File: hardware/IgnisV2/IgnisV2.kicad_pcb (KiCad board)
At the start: 2 copper layers, 50 x 50 mm, 82 parts, among them J1 COIL_A, J2 COIL_B, J3 530480210, J4 Conn_01x01_Pin, SW1 SW-18030, U1 BQ51013BRHLT, U2 BQ24073RGTR, U3 FP6277XR-G1, U4 74LVC1G17, U5 ATtiny212-SS

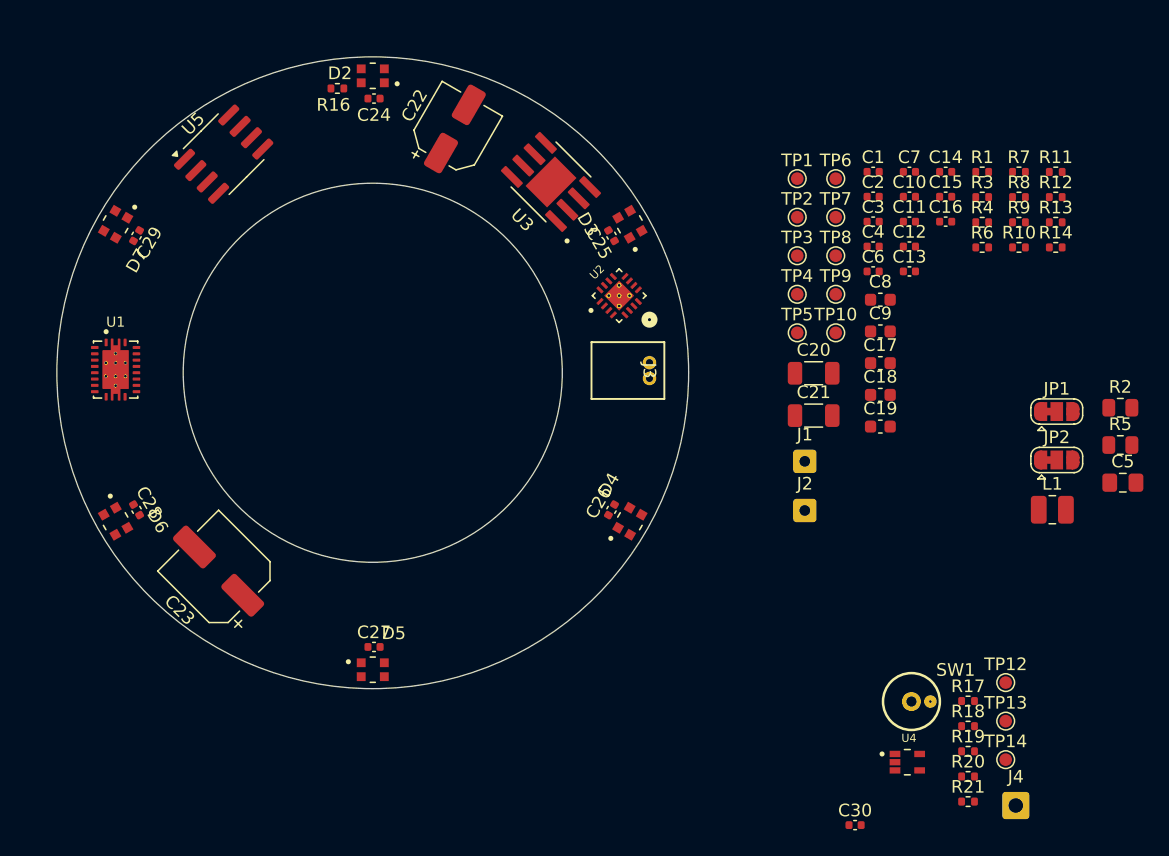
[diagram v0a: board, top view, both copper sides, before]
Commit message: 🏭 Finalize IgnisV2 PCB design and prepare for JLCPCB production
- Polished hierarchical schematics with clean signal routing
- Completed full PCB layout with optimized component placement
- Refined component selection for optimal JLCPCB compatibility
- Generated production files (Gerbers, drill, BOM, pick&place) for fabrication
- Exported 3D model snapshot for documentation and review
- Added 74LVC1G17 datasheet for package selection reference
- Selected TSSOP-5 package over SOT1202 for PCBA compatibility
- Configured for advanced PCBA service due to WS2812B backing requirements
- Updated design rules and gitignore for production workflow
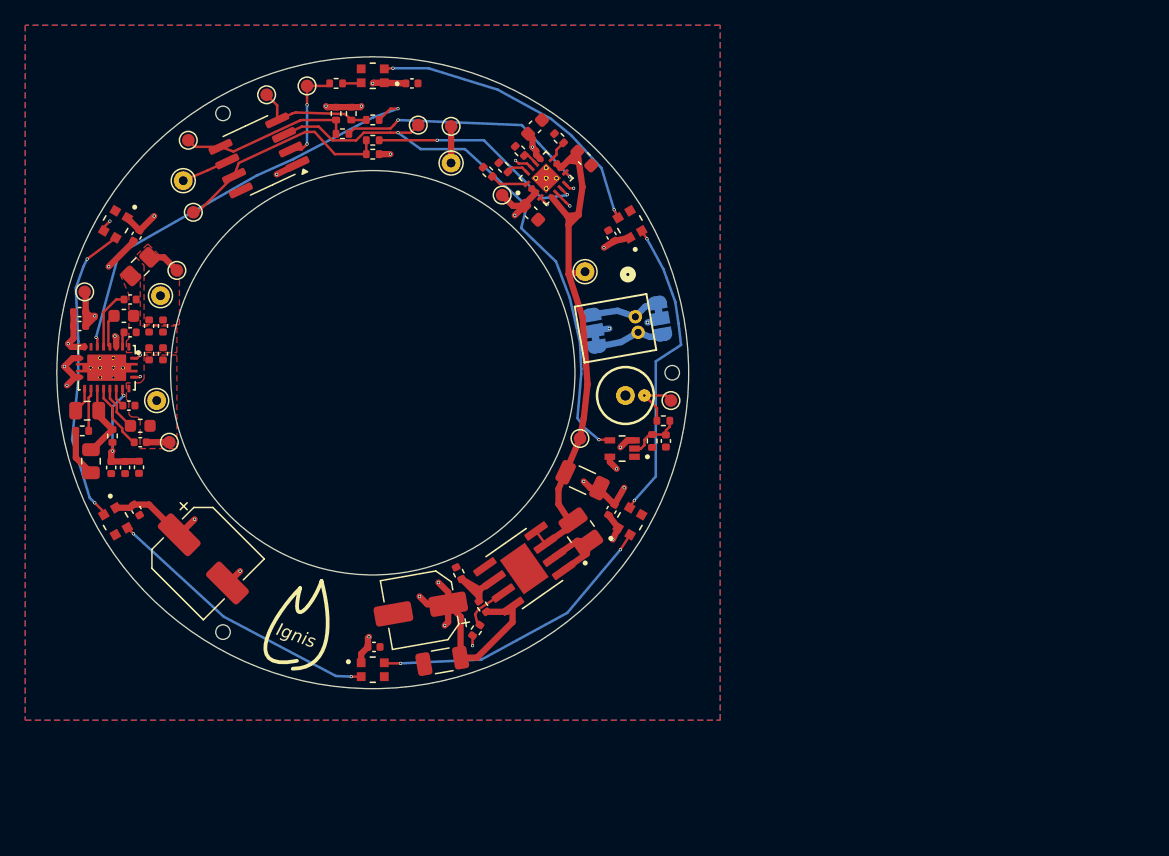
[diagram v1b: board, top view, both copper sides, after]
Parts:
- removed TP10: FB, TestPoint:TestPoint_Pad_D1.0mm
- added H1: ToolingHole, MountingHole:ToolingHole_1.152mm, F.Cu at (73.7, 50.0)
- added H2: ToolingHole, MountingHole:ToolingHole_1.152mm, F.Cu at (38.1, 70.5)
- added H3: ToolingHole, MountingHole:ToolingHole_1.152mm, F.Cu at (38.1, 29.5)
- added J5: VSYS, TestPoint:TestPoint_THTPad_D1.5mm_Drill0.7mm, F.Cu at (66.8, 42.0)
- added J6: GND, TestPoint:TestPoint_THTPad_D1.5mm_Drill0.7mm, F.Cu at (56.2, 33.4)
- J1, J2: footprint Connector_Wire:SolderWire-0.25sqmm_1x01_D0.65mm_OD1.7mm -> TestPoint:TestPoint_THTPad_D1.5mm_Drill0.7mm
- J4: value Conn_01x01_Pin -> UPDI; footprint Connector_Wire:SolderWire-0.5sqmm_1x01_D0.9mm_OD2.1mm -> TestPoint:TestPoint_THTPad_D1.5mm_Drill0.7mm
- JP1: value VGNDC -> VBATS; moved to B.Cu
- JP2: value VBATC -> VGNDS; moved to B.Cu
- moved J4 82.4 mm to (35.0, 34.8)
- moved R2 81.8 mm to (27.4, 53.0)
- moved R5 81.5 mm to (27.7, 57.0), turned to -90 degrees
- moved C5 79.6 mm to (31.6, 41.6), turned to -135 degrees
- moved R3 73.6 mm to (27.0, 54.6), turned to 180 degrees
- moved TP12 72.7 mm to (44.8, 27.3)
- moved R20 72.5 mm to (47.1, 29.5), turned to -90 degrees
- moved R4 70.9 mm to (29.4, 55.0), turned to 90 degrees
- moved R19 70.2 mm to (48.3, 29.5), turned to -90 degrees
- moved R21 69.6 mm to (50.0, 32.7), turned to 180 degrees
- moved C15 69.3 mm to (26.8, 46.3), turned to 180 degrees
- moved C16 68.9 mm to (26.8, 45.2), turned to 180 degrees
- moved TP14 68.4 mm to (53.6, 30.4)
- moved C14 68.0 mm to (31.5, 57.5), turned to -90 degrees
- moved C13 65.1 mm to (29.3, 57.5), turned to -90 degrees
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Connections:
- net Net-(J1-Pin_1) renamed /Power Stage/COILA
- net Net-(J2-Pin_1) renamed /Power Stage/AC2
- net Net-(JP1-C) renamed VBAT
- net Net-(U1-AC1) renamed /Power Stage/AC1
- J3 pad 1: Net-(JP1-A) -> Net-(J3-GND)
- J3 pad 2: Net-(JP1-B) -> Net-(J3-VBAT)
- JP1 pad 1: Net-(JP1-A) -> Net-(J3-VBAT)
- JP1 pad 3: Net-(JP1-B) -> Net-(J3-GND)
- JP2 pad 1: Net-(JP1-B) -> Net-(J3-GND)
- JP2 pad 3: Net-(JP1-A) -> Net-(J3-VBAT)
- R21 pad 2: ~{STBY} -> ~{PGOOD}
- R9 pad 2: ~{STBY} -> ~{PGOOD}
- TP12 pad 1: Net-(D2-DIN) -> LED_DIN
- U2 pad 18: (no net) -> GND
- U2 pad 19: (no net) -> GND
- U2 pad 20: (no net) -> GND
- U2 pad 21: (no net) -> GND
- U2 pad 22: (no net) -> GND
- U5 pad 7: ~{STBY} -> ~{PGOOD}
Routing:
- net VBUS: track 0.00 -> 55.9 mm, vias 0 -> 3
- net VCC: track 0.00 -> 46.8 mm, vias 0 -> 14
- net SSW: track 0.00 -> 45.7 mm, vias 0 -> 2
- net VSYS: track 0.00 -> 42.7 mm
- net Net-(U1-~{CHG}): track 0.00 -> 34.4 mm, vias 0 -> 2
- net GND: track 0.00 -> 33.6 mm, vias 0 -> 17
- net Net-(D3-DOUT): track 0.00 -> 24.4 mm, vias 0 -> 2
- net Net-(D6-DOUT): track 0.00 -> 24.0 mm, vias 0 -> 2
- net Net-(D2-DOUT): track 0.00 -> 23.8 mm, vias 0 -> 2
- net Net-(D4-DOUT): track 0.00 -> 23.4 mm, vias 0 -> 2
- net Net-(D5-DOUT): track 0.00 -> 22.4 mm, vias 0 -> 2
- net Net-(U2-~{CHG}): track 0.00 -> 20.3 mm, vias 0 -> 2
- net VBAT: track 0.00 -> 18.2 mm, vias 0 -> 2
- net ~{PGOOD}: track 0.00 -> 18.0 mm
- net Net-(U2-~{PGOOD}): track 0.00 -> 17.5 mm, vias 0 -> 2
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- added copper zone on F.Cu, net /Power Stage/AC1
- added copper zone on F.Cu, net /Power Stage/AC2
- added copper zone on F.Cu, net /Power Stage/COILA
- added copper zone on B.Cu, net GND
- added copper zone on F.Cu, net GND
- added copper zone on In1.Cu, net GND
- added copper zone on In2.Cu, net VBUS
- added copper zone on In2.Cu, net VCC
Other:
- outline, holes or cut-outs redrawn
- copper layers 2 -> 4
- board text added: "Ignis"
- board text added: "Ignis - V2.0 Théo - 2025-08-25"

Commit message: 🚨 Fix critical PCB issues caught during JLCPCB review
- Fixed undersized vias (<0.3mm) in component footprints to avoid extra costs
- Corrected WS2812B symbol pinout mismatch between standard and 2020 package
- Updated WS2812B-2020 wiring to match proper pin assignments
- Regenerated production files with corrected drill sizes and routing

**Critical catch: WS2812B standard vs 2020 package have different pinouts!**

Production halted and corrected before fabrication.
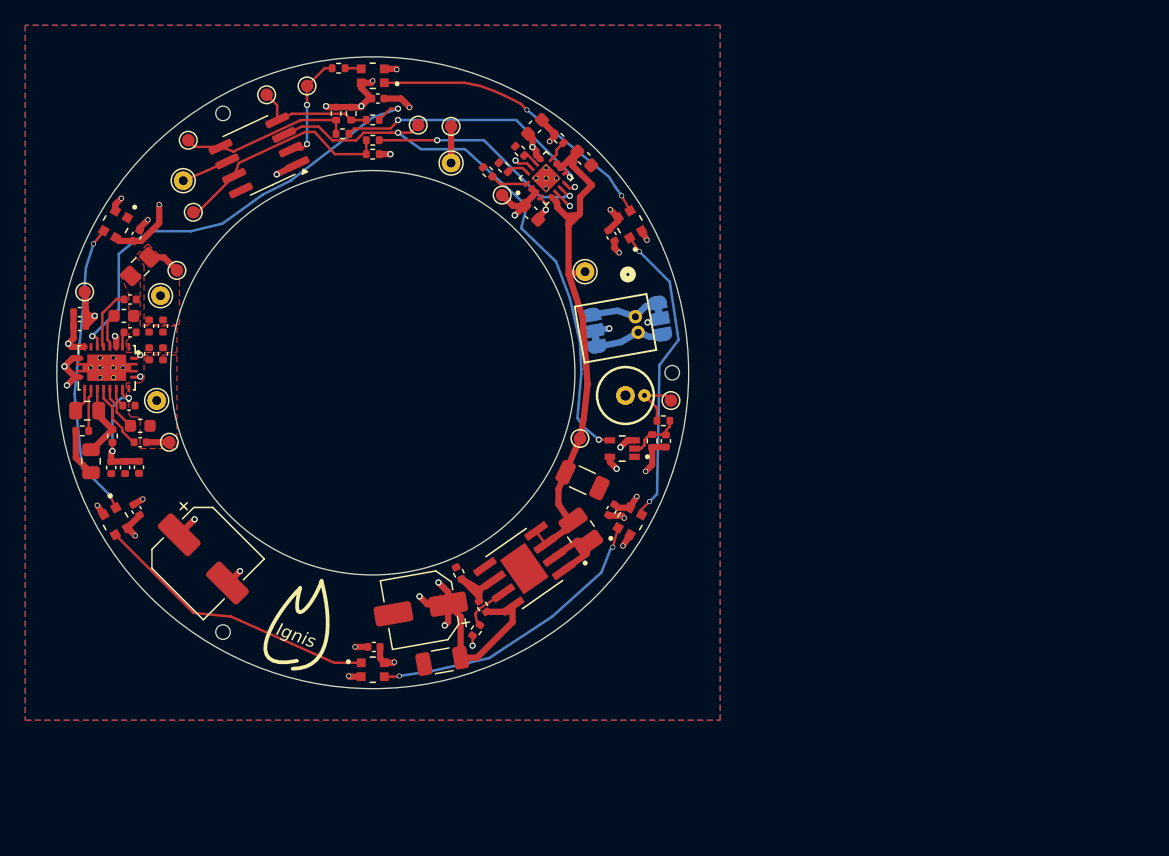
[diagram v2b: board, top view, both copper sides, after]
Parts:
- moved C24 2.95 mm to (50.4, 28.3)
- moved R16 1.22 mm to (47.3, 25.9)
- turned C25 to -60 degrees
- turned C26 to -120 degrees
- turned C27 to 180 degrees
- turned C28 to 120 degrees
- turned C29 to 60 degrees
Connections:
- D2 pad 1: VCC -> Net-(D2-DOUT)
- D2 pad 2: Net-(D2-DOUT) -> GND
- D2 pad 3: GND -> Net-(D2-DIN)
- D2 pad 4: Net-(D2-DIN) -> VCC
- D3 pad 1: VCC -> Net-(D3-DOUT)
- D3 pad 2: Net-(D3-DOUT) -> GND
- D3 pad 3: GND -> Net-(D2-DOUT)
- D3 pad 4: Net-(D2-DOUT) -> VCC
- D4 pad 1: VCC -> Net-(D4-DOUT)
- D4 pad 2: Net-(D4-DOUT) -> GND
- D4 pad 3: GND -> Net-(D3-DOUT)
- D4 pad 4: Net-(D3-DOUT) -> VCC
- D5 pad 1: VCC -> Net-(D5-DOUT)
- D5 pad 2: Net-(D5-DOUT) -> GND
- D5 pad 3: GND -> Net-(D4-DOUT)
- D5 pad 4: Net-(D4-DOUT) -> VCC
- D6 pad 1: VCC -> Net-(D6-DOUT)
- D6 pad 2: Net-(D6-DOUT) -> GND
- D6 pad 3: GND -> Net-(D5-DOUT)
- D6 pad 4: Net-(D5-DOUT) -> VCC
- D7 pad 1: VCC -> unconnected-(D7-DOUT-Pad1)
- D7 pad 2: unconnected-(D7-DOUT-Pad2) -> GND
- D7 pad 3: GND -> Net-(D6-DOUT)
- D7 pad 4: Net-(D6-DOUT) -> VCC
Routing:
- net GND: track 33.6 -> 45.7 mm, vias 17 -> 27
- net Net-(U1-~{CHG}): track 34.4 -> 35.9 mm
- net VSYS: track 42.7 -> 44.1 mm
- net Net-(U1-RECT): track 9.12 -> 9.92 mm
- net LED_DIN: track 7.94 -> 8.64 mm
- net Net-(D6-DOUT): track 24.0 -> 23.4 mm
- net Net-(D5-DOUT): track 22.4 -> 22.8 mm, vias 2 -> 0
- net VCC: track 46.8 -> 46.5 mm, vias 14 -> 15
